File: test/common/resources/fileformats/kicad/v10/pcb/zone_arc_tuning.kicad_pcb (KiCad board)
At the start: 2 copper layers, 100 x 90 mm, 0 parts

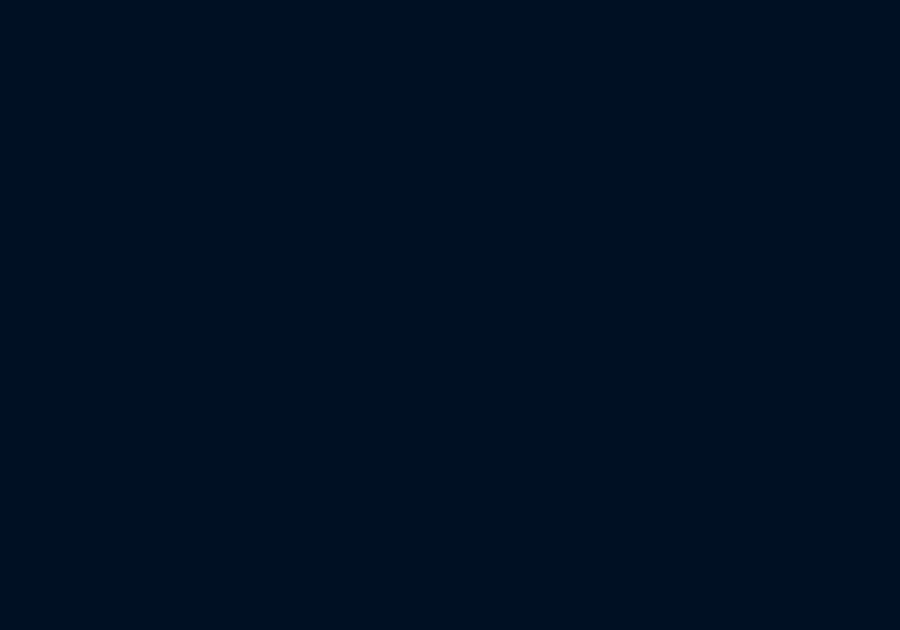
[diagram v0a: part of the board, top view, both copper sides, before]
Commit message: review lane: render-model center-dimension crash, room-binding oracle blindness, inter-room pull dedup
Four verified findings from the e3010ef8..HEAD adversarial review:

1. pcb_manager._extract_global_texts crashed with AttributeError on any
   board carrying a (dimension (type center)) — Dimension.gr_text became
   optional in-range (center dimensions carry no text, KiCad 10.0.3 writer
   :983-984) but the loop dereferenced it unconditionally, so the layout
   editor could not open such boards at all. Guarded with a skip; regression
   test constructs a center dimension via the API and demands
   get_render_model succeeds (burned with AttributeError pre-fix).

2. semantic_view projected zone placement as source_type/source — the
   by-design-always-None in-memory fields — so the D5 rule-area room binding
   ((sheetname X) | (component_class X)) was invisible to every oracle:
   rename, class->sheetname swap, and source-drop all left the view
   byte-identical. Now projects enabled + sheetname + component_class (an
   absent source token canonicalizes to sheetname "", KiCad's parser
   default, keeping v9/v10 cross-dialect equivalence). Footprint projection
   gains component_classes (sorted; KiCad treats membership as a set).
   SEMANTIC_VIEW_VERSION stays at 3 (already bumped by the pts lane this
   session); snapshots regenerated. zone_arc_tuning fixture now carries a
   component_class placement and a classed footprint; five new corrupter
   cases (class rename / token swap / source drop / class drop must move
   the view, class reorder must not) — all four breaking cases fail against
   the old projection (mutation-verified).

3. _pads_by_ref docstring scoped to translation: pad at x/y are
   footprint-relative but the angle is board-frame (includes footprint
   rotation, 10.0.3 writer :1688-1690), so only a pure move leaves the map
   untouched — prevents misdiagnosing a correct rewrite as data loss when
   extending the gate with rotation.

4. Repeated pull_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
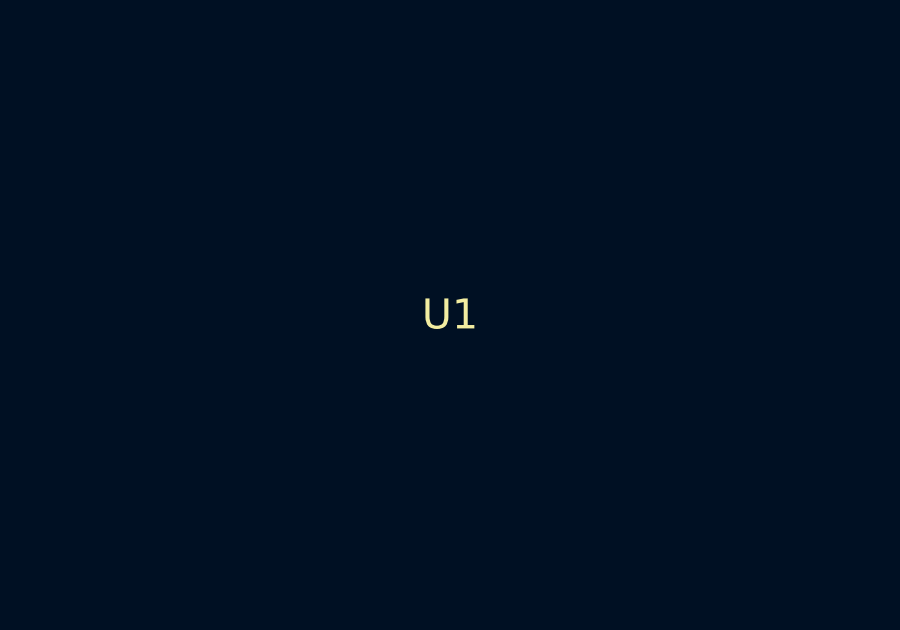
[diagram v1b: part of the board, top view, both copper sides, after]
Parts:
- added U1: , Corrupter:CLASSED, F.Cu at (60.0, 60.0)
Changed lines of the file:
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@@
 		(net "SIG")
+	)
+	(footprint "Corrupter:CLASSED"
+		(layer "F.Cu")
+		(at 60 60)
+		(property "Reference" "U1"
+			(at 0 -2 0)
+			(layer "F.SilkS")
+			(effects
+				(font
+					(size 1 1)
+					(thickness 0.15)
+				)
+			)
+		)
+		(component_classes
+			(class "PWR")
+			(class "ANALOG")
+		)
 	)
 	(zone
@@
 		)
 		(min_thickness 0.25)
+		(placement
+			(enabled yes)
+			(component_class "CLASSA")
+		)
 		(fill
 			(thermal_gap 0.5)
